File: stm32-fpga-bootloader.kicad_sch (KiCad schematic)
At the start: 77 parts, among them J1001 DATA, J1002 JTAG JUMP, J1003 JTAG-LOG, J1004 Conn_01x08, J15 Conn_01x02, J3 RPI-TO-CPLD, J5 PMOD, J6 Conn_01x02, J8 USB_C_Receptacle_USB2.0_14P, SW2 RUN, SW3 ICE_BTN, SW4 ICE_RST, U1 AMS1117-3.3, U13 ACPL-798J-500E, U4 ACPL-798J-500E

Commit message: Rework on pins assignements
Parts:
- JP1, JP2, JP3, JP4, JP5, JP6: footprint Connector_PinHeader_2.54mm:PinHeader_1x03_P2.54mm_Vertical -> Connector_PinSocket_1.27mm:PinSocket_1x03_P1.27mm_Vertical
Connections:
- net PB11B/PCLKC2_1: no longer JP6.3 (B)
- net PB15A: no longer JP2.3 (B)
- net PB15B: no longer JP4.3 (B)
- net PR10C: no longer JP1.3 (B)
- net PR10D: no longer JP5.3 (B)
- net PR8D: no longer JP3.3 (B)
- new net PR2A: JP2.3 (B)
- new net PR2B: JP4.3 (B)
- new net PR3A: JP6.3 (B)
- new net PR3B: JP1.3 (B)
- new net PR4A: JP3.3 (B)
- new net PR4B: JP5.3 (B)
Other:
- sheet lcmxo2-cpld-block ports: added PR2A, PR2B, PR3A, PR3B, PR4A, PR4B, PR4C, PR4D, PR5A, PR5B, PR5C/PCLKT1_0, PR5D/PCLKC1_0, PR9A, PR9B, PR9C, PR9D; removed CPLD_B4_PR9A
- moved on the sheet: JP1, JP2, JP3, JP4, JP5, JP6

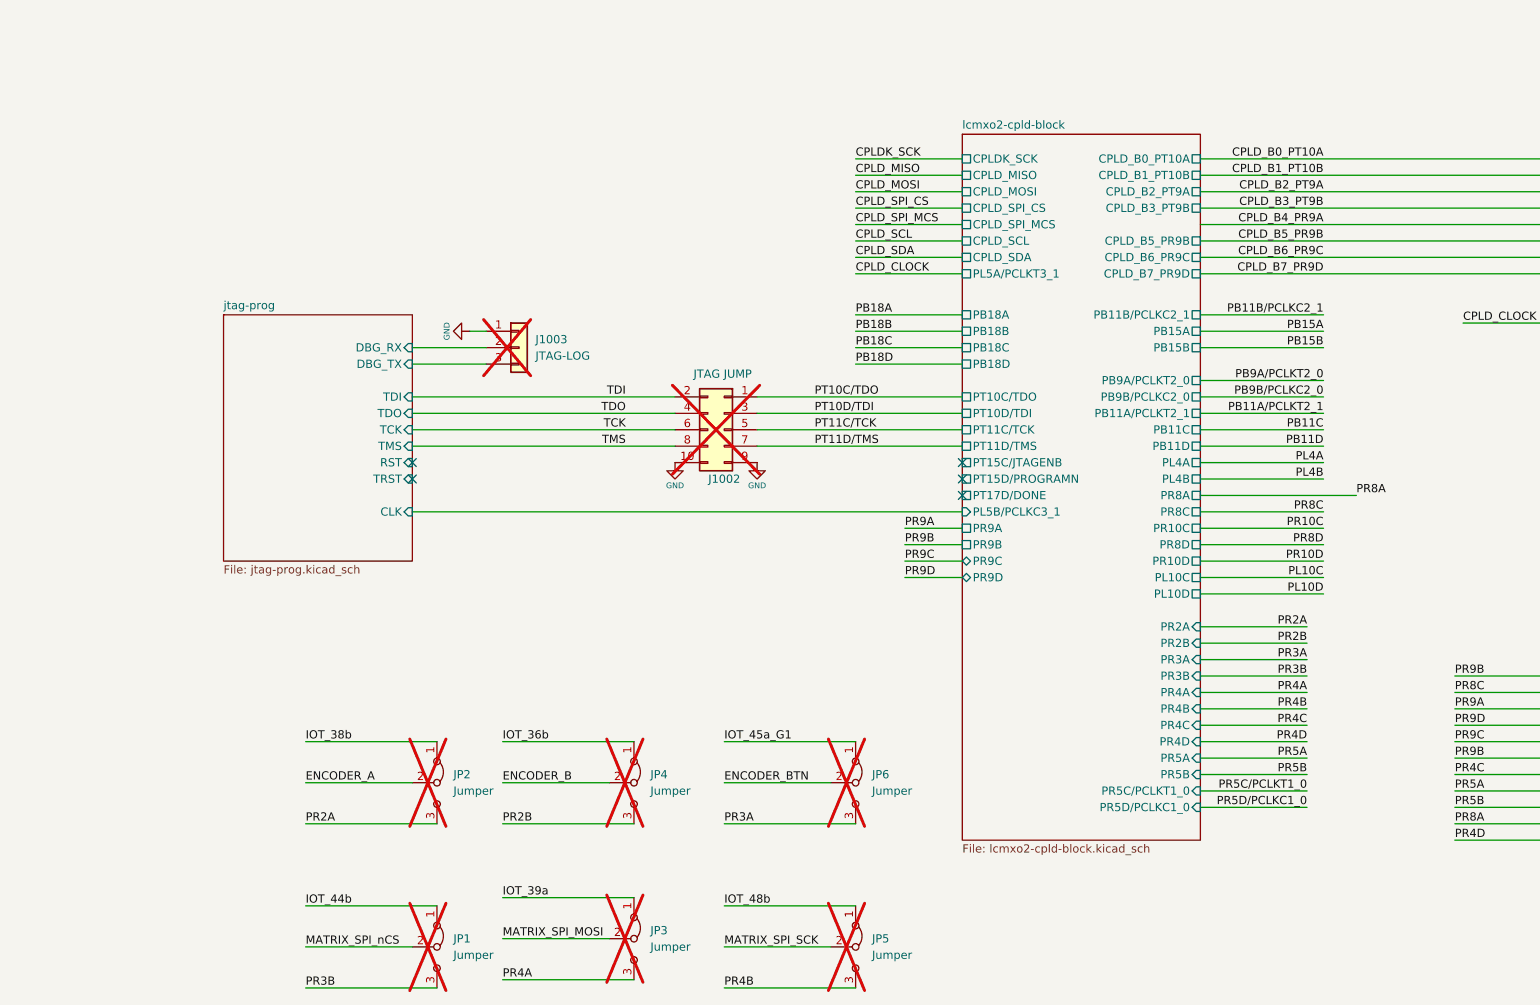
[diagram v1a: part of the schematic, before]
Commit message: Rework on pins assignements
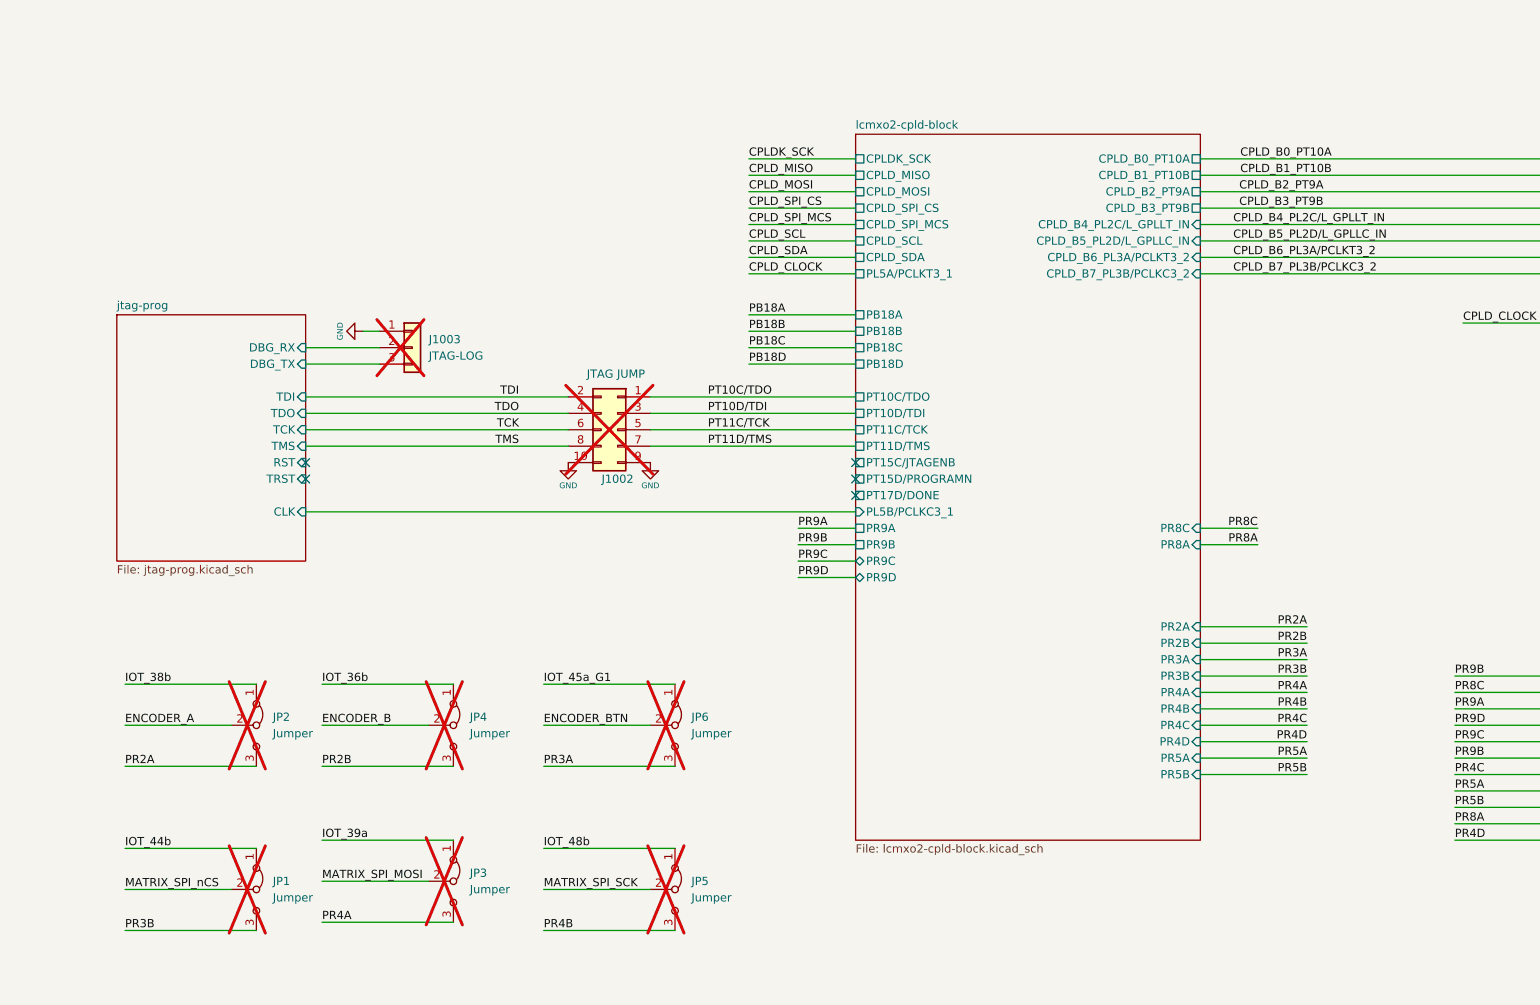
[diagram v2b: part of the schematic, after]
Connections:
- net CPLD_B4_PR9A renamed CPLD_B4_PL2C/L_GPLLT_IN
- net CPLD_B5_PR9B renamed CPLD_B5_PL2D/L_GPLLC_IN
- net CPLD_B6_PR9C renamed CPLD_B6_PL3A/PCLKT3_2
- net CPLD_B7_PR9D renamed CPLD_B7_PL3B/PCLKC3_2
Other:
- sheet lcmxo2-cpld-block ports: added CPLD_B4_PL2C/L_GPLLT_IN, CPLD_B5_PL2D/L_GPLLC_IN, CPLD_B6_PL3A/PCLKT3_2, CPLD_B7_PL3B/PCLKC3_2; removed CPLD_B5_PR9B, CPLD_B6_PR9C, CPLD_B7_PR9D, PB11A/PCLKT2_1, PB11B/PCLKC2_1, PB11C, PB11D, PB15A, PB15B, PB9A/PCLKT2_0, PB9B/PCLKC2_0, PL10C, PL10D, PL4A, PL4B, PR10C, PR10D, PR5C/PCLKT1_0, PR5D/PCLKC1_0, PR8D
- moved on the sheet: J1002, J1003, JP1, JP2, JP3, JP4, JP5, JP6

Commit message: Update the source code
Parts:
- removed C15, C48: 100n, Capacitor_SMD:C_0402_1005Metric, symbol Device:C_Small
- removed C16, C49: 10uF, Capacitor_SMD:C_0603_1608Metric, symbol Device:C_Small
- removed J1001: DATA, Connector_PinSocket_2.54mm:PinSocket_1x04_P2.54mm_Vertical, symbol Connector_Generic:Conn_01x04
- removed J15: Conn_01x02, Connector_PinSocket_2.54mm:PinSocket_1x02_P2.54mm_Vertical, symbol Connector_Generic:Conn_01x02
- removed J6: Conn_01x02, TerminalBlock_Phoenix:TerminalBlock_Phoenix_PT-1,5-2-3.5-H_1x02_P3.50mm_Horizontal, symbol Connector_Generic:Conn_01x02
- removed R23, R24, R25, R26, R27, R73, R74, R75, R76, R77: 1.2K, Resistor_SMD:R_0603_1608Metric, symbol Device:R_Small
- removed R30, R31, R33, R34, R35, R36, R78, R79, R80, R81, R82, R83: 100R, Resistor_SMD:R_0603_1608Metric, symbol Device:R_Small
- removed U13, U4: ACPL-798J-500E, EasyEDA_Lib:SO-16_L10.3-W7.5-P1.27-LS10.6-BL, symbol KiCadLocal:ACPL-798J-500E
- added J1005: JTAG JUMP, Connector_PinSocket_2.54mm:PinSocket_2x05_P2.54mm_Vertical, symbol Connector_Generic:Conn_02x05_Odd_Even
- A1, A2: footprint Module:RaspberryPi_Pico_Common_THT -> KiCadLocal:RaspberryPi_Pico_Common_THT
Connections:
- net GND: now also J1002.1 (Pin_1), J1002.2 (Pin_2), J1004.8 (Pin_8); no longer J1002.10 (Pin_10), J1002.9 (Pin_9)
- net IOB_13b: now also J1004.2 (Pin_2)
- net IOB_20a: now also J1004.4 (Pin_4)
- net IOB_22a: now also J1004.5 (Pin_5)
- net IOB_23b: now also J1004.6 (Pin_6)
- net IOT_37a: now also J1004.3 (Pin_3)
- net IOT_43a: now also J1004.7 (Pin_7)
- net IOT_50b: now also J1004.1 (Pin_1)
- net PT10C/TDO: now also J1002.9 (Pin_9); no longer J1002.1 (Pin_1)
- net PT10D/TDI: now also J1002.7 (Pin_7); no longer J1002.3 (Pin_3)
- net PT11D/TMS: now also J1002.3 (Pin_3); no longer J1002.7 (Pin_7)
- net TDI: now also J1002.10 (Pin_10); no longer J1002.2 (Pin_2)
- net TDO: now also J1002.8 (Pin_8); no longer J1002.4 (Pin_4)
- net TMS: now also J1002.4 (Pin_4); no longer J1002.8 (Pin_8)
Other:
- added sheet isolated-measurements (isolated-measurements.kicad_sch)
- sheet lcmxo2-cpld-block ports: added PR8D; removed none
- moved on the sheet: D1003, D1004, D3, J1002, J1004, R11

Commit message: Update the source code
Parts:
- removed J1005: JTAG JUMP, Connector_PinSocket_2.54mm:PinSocket_2x05_P2.54mm_Vertical, symbol Connector_Generic:Conn_02x05_Odd_Even
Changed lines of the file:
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@@
 			"AAAAAAAAAAAAAAAAAAAAAAAAAAAAAAAAAAAAAAAAAAAAAAAAAAAAAAAAAAAAAAAAAAAAAAAAAAAA"
 			"AAAAAAAAAAAAAAAAAAAAAAAAAAAAAAAAAAAAAAAAAAAAAAAAAAAAAAAAAAAAAAAAAAAAAAAAAAAA"
+			"AAAAAAAAAAAAAAAAAAAAAAAAAAAAAAAAAAAAAAAAAAAAAAAAAAAAAAAAAAAAAAAAAAAAAAAAAAAA"
+			"AAAAAAAAAAAAAAAAAAAAAAAAAAAAAAAAAAAAAAAAAAAAAAAAAAAAAAAAAAAAAAAAAAAAAAAAAAAA"
+			"AAAAAAAAAAAAAAAAAAAAAAAAAAAAAAAAAAAAAAAAAAAAAAAAAAAAAAAAAAAAAAAAAAAAAAAAAAAA"
+			"AAAAAAAAAAAAAAAAAAAAAAAAAAAAAAAAAAAAAAAAAAAAAAAAAAAAAAAAAAAAAAAAAAAAAAAAAAAA"
+			"AAAAAAAAAAAAAAAAAAAAAAAAAAAAAAAAAAAAAAAAAAAAAAAAAAAAAAAAAAAAAAAAAAAAAAAAAAAA"
+			"AAAAAAAAAAAAAAAAAAAAAAAAAAAAAAAAAAAAAAAAAAAAAAAAAAAAAAAAAAAAAAAAAAAAAAAAAAAA"
+			"AAAAAAAAAAAAAAAAAAAAAAAAAAAAAAAAAAAAAAAAAAAAAAAAAAAAAAAAAAAAAAAAAAAAAAAAAAAA"
+			"AAAAAAAAAAAAAAAAAAAAAAAAAAAAAAAAAAAAAAAAAAAAAAAAAAAAAAAAAAAAAAAAAAAAAAAAAAAA"
+			"AAAAAAAAAAAAAAAAAAAAAAAAAAAAAAAAAAAAAAAAAAAAAAAAAAAAAAAAAAAAAAAAAAAAAAAAAAAA"
+			"AAAAAAAAAAAAAAAAAAAAAAAAAAAAAAAAAAAAAAAAAAAAAAAAAAAAAAAAAAAAAAAAAAAAAAAAAAAA"
+			"AAAAAAAAAAAAAAAAAAAAAAAAAAAAAAAAAAAAAAAAAAAAAAAAAAAAAAAAAAAAAAAAAAAAAAAAAAAA"
+			"AAAAAAAAAAAAAAAAAAAAAAAAAAAAAAAAAAAAAAAAAAAAAAAAAAAAAAAAAAAAAAAAAAAAAAAAAAAA"
+			"AAAAAAAAAAAAAAAAAAAAAAAAAAAAAAAAAAAAAAAAAAAAAAAAAAAAAAAAAAAAAAAAAAAAAAAAAAAA"
+			"AAAAAAAAAAAAAAAAAAAAAAAAAAAAAAAAAAAAAAAAAAAAAAAAAAAAAAAAAAAAAAAAAAAAAAAAAAAA"
+			"AAAAAAAAAAAAAAAAAAAAAAAAAAAAAAAAAAAAAAAAAAAAAAAAAAAAAAAAAAAAAAAAAAAAAAAAAAAA"
+			"AAAAAAAAAAAAAAAAAAAAAAAAAAAAAAAAAAAAAAAAAAAAAAAAAAAAAAAAAAAAAAAAAAAAAAAAAAAA"
+			"AAAAAAAAAAAAAAAAAAAAAAAAAAAAAAAAAAAAAAAAAAAAAAAAAAAAAAAAAAAAAAAAAAAAAAAAAAAA"
+			"AAAAAAAAAAAAAAAAAAAAAAAAAAAAAAAAAAAAAAAAAAAAAAAAAAAAAAAAAAAAAAAAAAAAAAAAAAAA"
 			"AAAAAAAAAAAAAAAAAAAAAAAAAAAAAAAAAAAAAAAAAAAAAAAAAAAAAA=="
 		)
@@
 					(unit 1)
 				)
-			)
-		)
-	)
-	(symbol
-		(lib_id "Connector_Generic:Conn_02x05_Odd_Even")
-		(at 264.16 238.76 180)
-		(unit 1)
-		(exclude_from_sim no)
-		(in_bom no)
-		(on_board yes)
-		(dnp yes)
-		(property "Reference" "J1005"
-			(at 264.16 231.14 0)
-			(effects
-				(font
-					(size 1.27 1.27)
-				)
-			)
-		)
-		(property "Value" "JTAG JUMP"
-			(at 263.906 247.396 0)
-			(effects
-				(font
-					(size 1.27 1.27)
-				)
-			)
-		)
-		(property "Footprint" "Connector_PinSocket_2.54mm:PinSocket_2x05_P2.54mm_Vertical"
-			(at 264.16 215.392 0)
-			(effects
-				(font
-					(size 1.27 1.27)
-				)
-				(hide yes)
-			)
-		)
-		(property "Datasheet" "~"
-			(at 264.16 238.76 0)
-			(effects
-				(font
-					(size 1.27 1.27)
-				)
-				(hide yes)
-			)
-		)
-		(property "Description" "Generic connector, double row, 02x05, odd/even pin numbering scheme (row 1 odd numbers, row 2 even numbers), script generated (kicad-library-utils/schlib/autogen/connector/)"
-			(at 264.16 238.76 0)
-			(effects
-				(font
-					(size 1.27 1.27)
-				)
-				(hide yes)
-			)
-		)
-		(pin "6"
-		)
-		(pin "3"
-		)
-		(pin "10"
-		)
-		(pin "4"
-		)
-		(pin "7"
-		)
-		(pin "1"
-		)
-		(pin "9"
-		)
-		(pin "8"
-		)
-		(pin "5"
-		)
-		(pin "2"
-		)
-		(instances
-			(project "stm32-fpga-bootloader"
-				(path "/5ed49623-6cbc-4a61-8fb3-1814d185ddb6"
-					(reference "J1005")
-					(unit 1)
-				)
